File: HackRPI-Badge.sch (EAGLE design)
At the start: 41 parts, among them J1 FTDI_BASICPTH, J2 SOLDERJUMPERTRACE-PTH, U2 3.3V, U4 74595, U5 74595, U6 74595, U7 74165DT

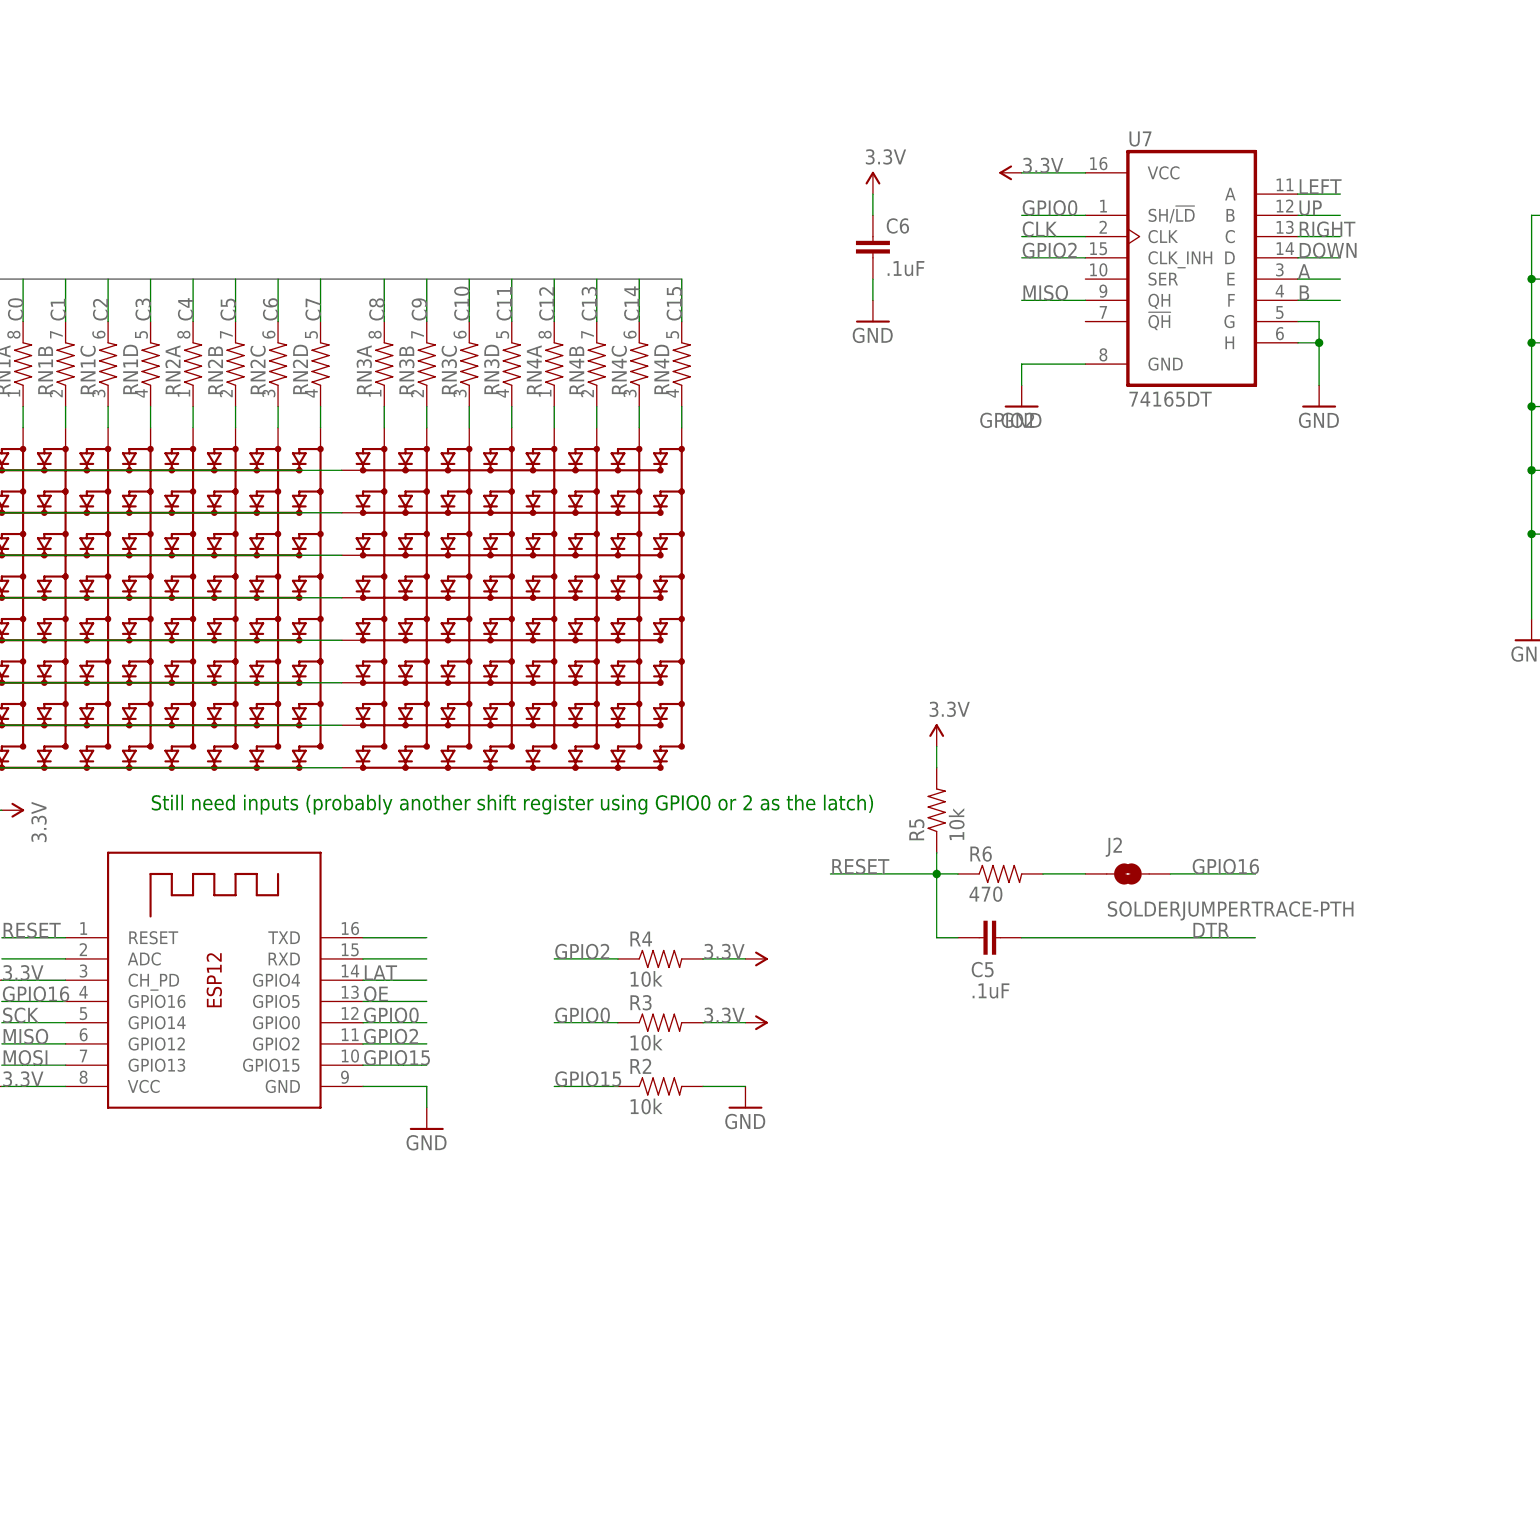
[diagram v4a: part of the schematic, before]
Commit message: Added flash memory for storing certificates, named some nets to be more clear
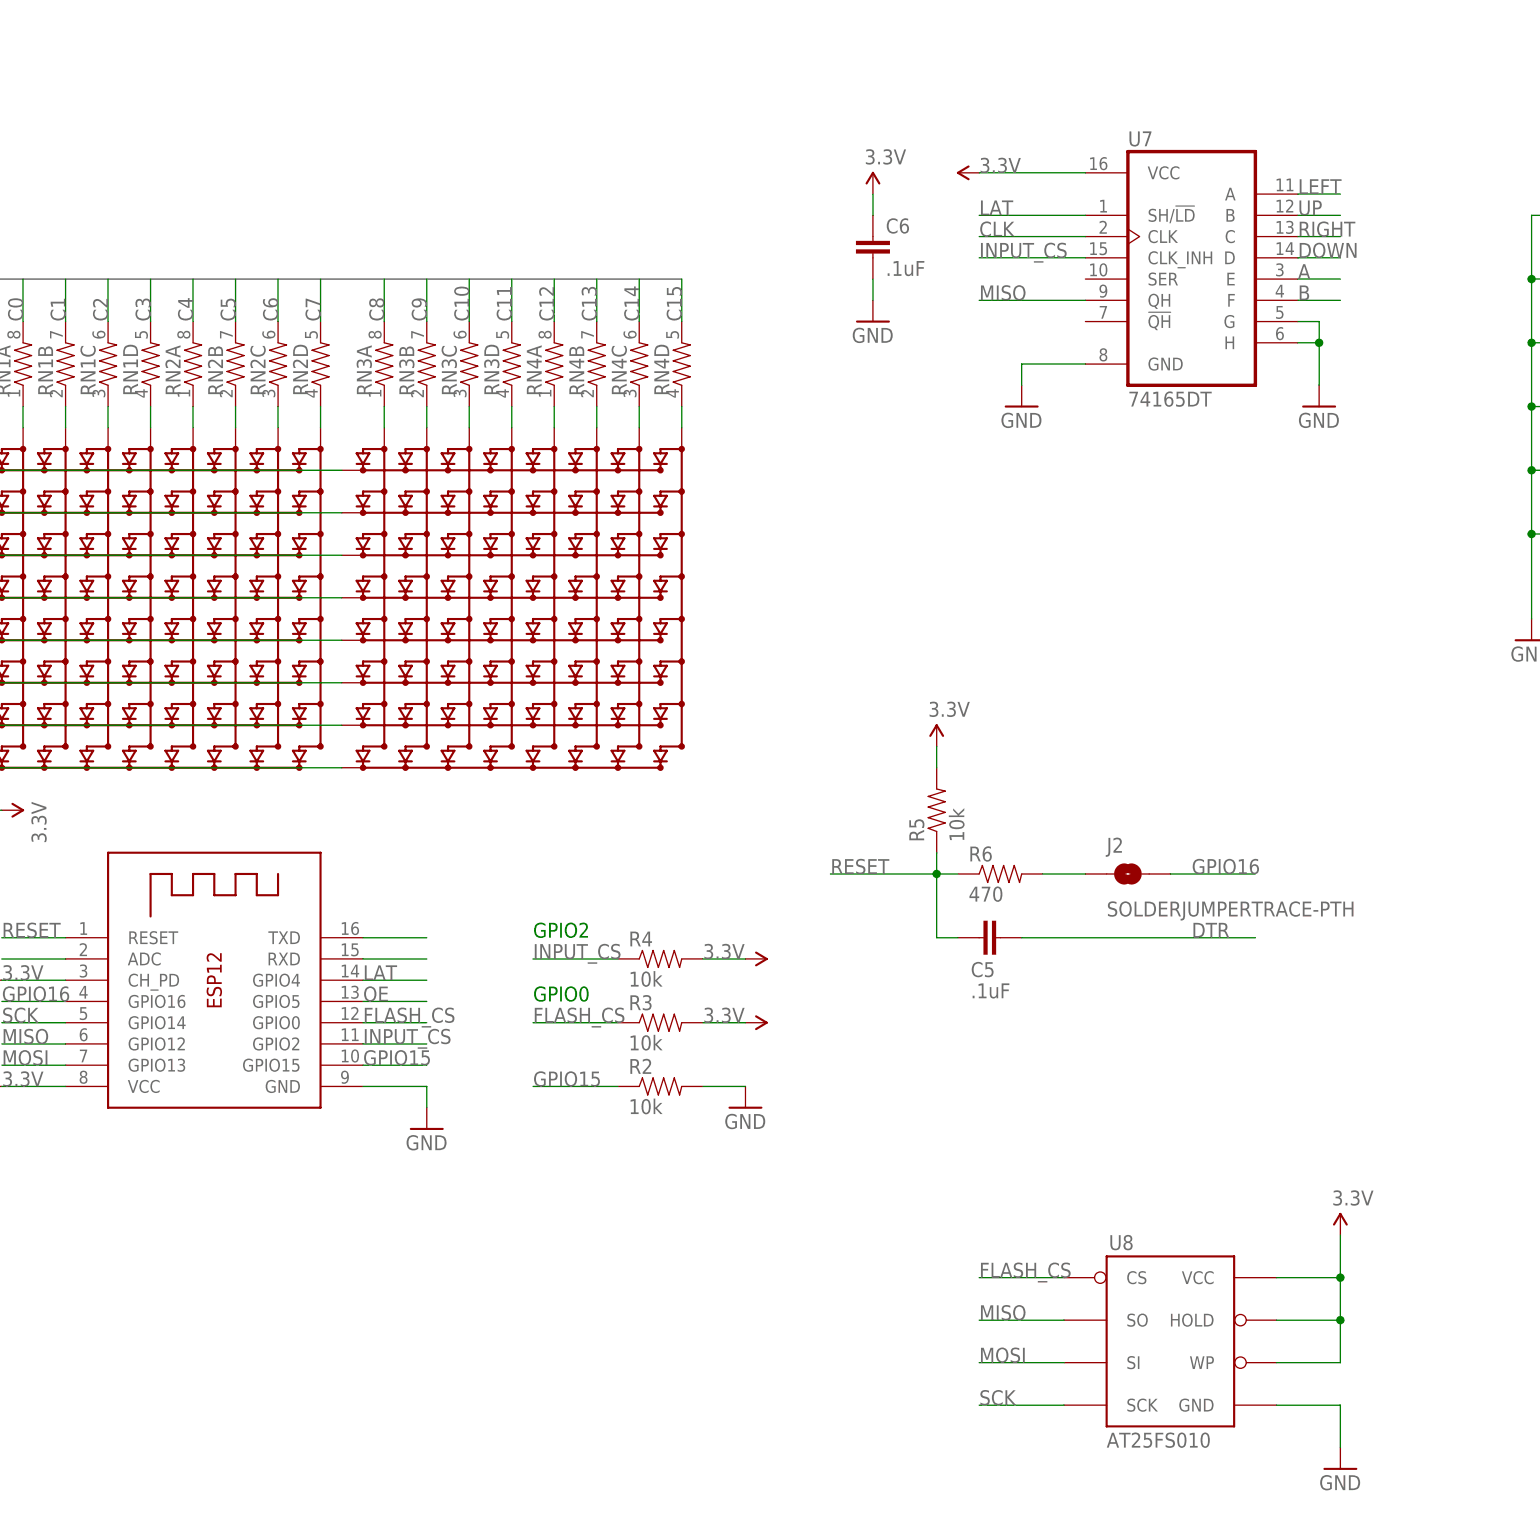
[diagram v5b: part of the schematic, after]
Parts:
- added U8: AT25FS010, SparkFun-DigitalIC:AT25FS010
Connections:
- net GPIO2 renamed INPUT_CS
- removed net GPIO0: R3.1, U1.GPIO0, U7.SH/!LD
- new net FLASH_CS: R3.1, U1.GPIO0, U8.CS
- net 3.3V: now also U8.HOLD, U8.VCC, U8.WP
- net GND: now also U8.GND
- net LAT: now also U7.SH/!LD
- net MISO: now also U8.SO
- net MOSI: now also U8.SI
- net SCK: now also U8.SCK
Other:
- note added: "GPIO0"
- note added: "GPIO2"
- note removed: "Still need inputs (probably another shift register using GPIO0 or 2 as the latch)"
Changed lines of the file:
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@@
 <part name="GND17" library="SparkFun-Aesthetics" deviceset="GND" device=""/>
 <part name="SUPPLY23" library="SparkFun-Aesthetics" deviceset="V_BATT" device=""/>
+<part name="SUPPLY24" library="SparkFun-Aesthetics" deviceset="3.3V" device=""/>
+<part name="GND18" library="SparkFun-Aesthetics" deviceset="GND" device=""/>
+<part name="U8" library="SparkFun-DigitalIC" deviceset="AT25FS010" device=""/>
 </parts>
 <sheets>
 <sheet>
 <plain>
-<text x="-7.62" y="20.32" size="1.778" layer="91">Still need inputs (probably another shift register using GPIO0 or 2 as the latch)</text>
+<text x="38.1" y="-2.54" size="1.778" layer="91">GPIO0</text>
+<text x="38.1" y="5.08" size="1.778" layer="91">GPIO2</text>
 </plain>
 <instances>
@@
 </instance>
 <instance part="GND13" gate="1" x="157.48" y="40.64"/>
-<instance part="SUPPLY20" gate="G$1" x="96.52" y="96.52" smashed="yes" rot="R90">
-<attribute name="VALUE" x="96.52" y="96.52" size="1.778" layer="96"/>
+<instance part="SUPPLY20" gate="G$1" x="91.44" y="96.52" smashed="yes" rot="R90">
+<attribute name="VALUE" x="91.44" y="96.52" size="1.778" layer="96"/>
 </instance>
 <instance part="GND14" gate="1" x="96.52" y="68.58"/>
@@
 <instance part="GND17" gate="1" x="-190.5" y="12.7"/>
 <instance part="SUPPLY23" gate="G$1" x="-190.5" y="45.72"/>
+<instance part="SUPPLY24" gate="G$1" x="134.62" y="-30.48"/>
+<instance part="GND18" gate="1" x="134.62" y="-58.42"/>
+<instance part="U8" gate="G$1" x="114.3" y="-40.64"/>
 </instances>
 <busses>
@@
 <label x="-119.38" y="134.62" size="1.778" layer="95"/>
 </segment>
+<segment>
+<wire x1="101.6" y1="-50.8" x2="91.44" y2="-50.8" width="0.1524" layer="91"/>
+<label x="91.44" y="-50.8" size="1.778" layer="95"/>
+<pinref part="U8" gate="G$1" pin="SCK"/>
+</segment>
 </net>
 <net name="MISO" class="0">
@@
 <segment>
 <pinref part="U7" gate="A" pin="QH"/>
-<wire x1="104.14" y1="81.28" x2="96.52" y2="81.28" width="0.1524" layer="91"/>
-<label x="96.52" y="81.28" size="1.778" layer="95"/>
+<wire x1="104.14" y1="81.28" x2="91.44" y2="81.28" width="0.1524" layer="91"/>
+<label x="91.44" y="81.28" size="1.778" layer="95"/>
+</segment>
+<segment>
+<wire x1="91.44" y1="-40.64" x2="101.6" y2="-40.64" width="0.1524" layer="91"/>
+<label x="91.44" y="-40.64" size="1.778" layer="95"/>
+<pinref part="U8" gate="G$1" pin="SO"/>
 </segment>
 </net>
@@
 <wire x1="-111.76" y1="172.72" x2="-119.38" y2="172.72" width="0.1524" layer="91"/>
 <label x="-119.38" y="172.72" size="1.778" layer="95"/>
+</segment>
+<segment>
+<wire x1="101.6" y1="-45.72" x2="91.44" y2="-45.72" width="0.1524" layer="91"/>
+<label x="91.44" y="-45.72" size="1.778" layer="95"/>
+<pinref part="U8" gate="G$1" pin="SI"/>
 </segment>
 </net>
@@
 <segment>
 <pinref part="U7" gate="A" pin="VCC"/>
-<wire x1="104.14" y1="96.52" x2="96.52" y2="96.52" width="0.1524" layer="91"/>
+<wire x1="104.14" y1="96.52" x2="91.44" y2="96.52" width="0.1524" layer="91"/>
 <pinref part="SUPPLY20" gate="G$1" pin="3.3V"/>
 </segment>
@@
 <pinref part="SUPPLY22" gate="G$1" pin="3.3V"/>
 <wire x1="-88.9" y1="53.34" x2="-88.9" y2="50.8" width="0.1524" layer="91"/>
+</segment>
+<segment>
+<wire x1="127" y1="-35.56" x2="134.62" y2="-35.56" width="0.1524" layer="91"/>
+<wire x1="134.62" y1="-35.56" x2="134.62" y2="-30.48" width="0.1524" layer="91"/>
+<pinref part="SUPPLY24" gate="G$1" pin="3.3V"/>
+<wire x1="127" y1="-45.72" x2="134.62" y2="-45.72" width="0.1524" layer="91"/>
+<wire x1="134.62" y1="-45.72" x2="134.62" y2="-40.64" width="0.1524" layer="91"/>
+<junction x="134.62" y="-35.56"/>
+<pinref part="U8" gate="G$1" pin="WP"/>
+<pinref part="U8" gate="G$1" pin="VCC"/>
+<pinref part="U8" gate="G$1" pin="HOLD"/>
+<wire x1="134.62" y1="-40.64" x2="134.62" y2="-35.56" width="0.1524" layer="91"/>
+<wire x1="127" y1="-40.64" x2="134.62" y2="-40.64" width="0.1524" layer="91"/>
+<junction x="134.62" y="-40.64"/>
 </segment>
 </net>
@@
 <pinref part="GND17" gate="1" pin="GND"/>
 </segment>
-</net>
-<net name="GPIO2" class="0">
+<segment>
+<wire x1="127" y1="-50.8" x2="134.62" y2="-50.8" width="0.1524" layer="91"/>
+<wire x1="134.62" y1="-50.8" x2="134.62" y2="-55.88" width="0.1524" layer="91"/>
+<pinref part="GND18" gate="1" pin="GND"/>
+<pinref part="U8" gate="G$1" pin="GND"/>
+</segment>
+</net>
+<net name="INPUT_CS" class="0">
 <segment>
 <pinref part="U1" gate="G$1" pin="GPIO2"/>
@@
 </segment>
 <segment>
-<wire x1="40.64" y1="2.54" x2="48.26" y2="2.54" width="0.1524" layer="91"/>
+<wire x1="38.1" y1="2.54" x2="48.26" y2="2.54" width="0.1524" layer="91"/>
 <pinref part="R4" gate="G$1" pin="1"/>
-<label x="40.64" y="2.54" size="1.778" layer="95"/>
+<label x="38.1" y="2.54" size="1.778" layer="95"/>
 </segment>
 <segment>
 <pinref part="U7" gate="A" pin="CLK_INH"/>
-<wire x1="104.14" y1="86.36" x2="96.52" y2="86.36" width="0.1524" layer="91"/>
-<label x="91.44" y="66.04" size="1.778" layer="95"/>
-<label x="96.52" y="86.36" size="1.778" layer="95"/>
-</segment>
-</net>
-<net name="GPIO0" class="0">
+<wire x1="104.14" y1="86.36" x2="91.44" y2="86.36" width="0.1524" layer="91"/>
+<label x="91.44" y="86.36" size="1.778" layer="95"/>
+</segment>
+</net>
+<net name="FLASH_CS" class="0">
 <segment>
 <pinref part="U1" gate="G$1" pin="GPIO0"/>
@@
 </segment>
 <segment>
-<wire x1="40.64" y1="-5.08" x2="48.26" y2="-5.08" width="0.1524" layer="91"/>
+<wire x1="38.1" y1="-5.08" x2="48.26" y2="-5.08" width="0.1524" layer="91"/>
 <pinref part="R3" gate="G$1" pin="1"/>
-<label x="40.64" y="-5.08" size="1.778" layer="95"/>
-</segment>
-<segment>
-<pinref part="U7" gate="A" pin="SH/!LD"/>
-<wire x1="104.14" y1="91.44" x2="96.52" y2="91.44" width="0.1524" layer="91"/>
-<label x="96.52" y="91.44" size="1.778" layer="95"/>
+<label x="38.1" y="-5.08" size="1.778" layer="95"/>
+</segment>
+<segment>
+<wire x1="101.6" y1="-35.56" x2="91.44" y2="-35.56" width="0.1524" layer="91"/>
+<label x="91.44" y="-35.56" size="1.778" layer="95"/>
+<pinref part="U8" gate="G$1" pin="CS"/>
 </segment>
 </net>
@@
 <label x="17.78" y="0" size="1.778" layer="95"/>
 </segment>
+<segment>
+<pinref part="U7" gate="A" pin="SH/!LD"/>
+<wire x1="104.14" y1="91.44" x2="91.44" y2="91.44" width="0.1524" layer="91"/>
+<label x="91.44" y="91.44" size="1.778" layer="95"/>
+</segment>
 </net>
 <net name="OE" class="0">
@@
 <segment>
 <pinref part="R2" gate="G$1" pin="1"/>
-<wire x1="48.26" y1="-12.7" x2="40.64" y2="-12.7" width="0.1524" layer="91"/>
-<label x="40.64" y="-12.7" size="1.778" layer="95"/>
+<wire x1="48.26" y1="-12.7" x2="38.1" y2="-12.7" width="0.1524" layer="91"/>
+<label x="38.1" y="-12.7" size="1.778" layer="95"/>
 </segment>
 </net>
@@
 <segment>
 <pinref part="U7" gate="A" pin="CLK"/>
-<wire x1="104.14" y1="88.9" x2="96.52" y2="88.9" width="0.1524" layer="91"/>
-<label x="96.52" y="88.9" size="1.778" layer="95"/>
-</segment>
-</net>
+<wire x1="104.14" y1="88.9" x2="91.44" y2="88.9" width="0.1524" layer="91"/>
+<label x="91.44" y="88.9" size="1.778" layer="95"/>
+</segment>
+</net>
